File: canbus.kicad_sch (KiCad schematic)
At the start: 12 parts, among them U1 MCP2562FD, U2 MCP2518FD, Y1 40 MHz

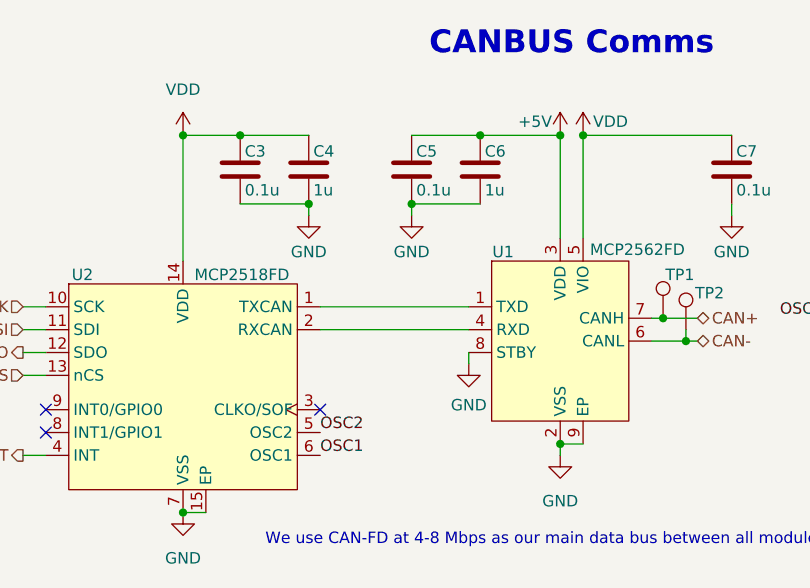
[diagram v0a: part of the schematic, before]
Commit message: Update MCP symbols to remove Exposed Pad pin.
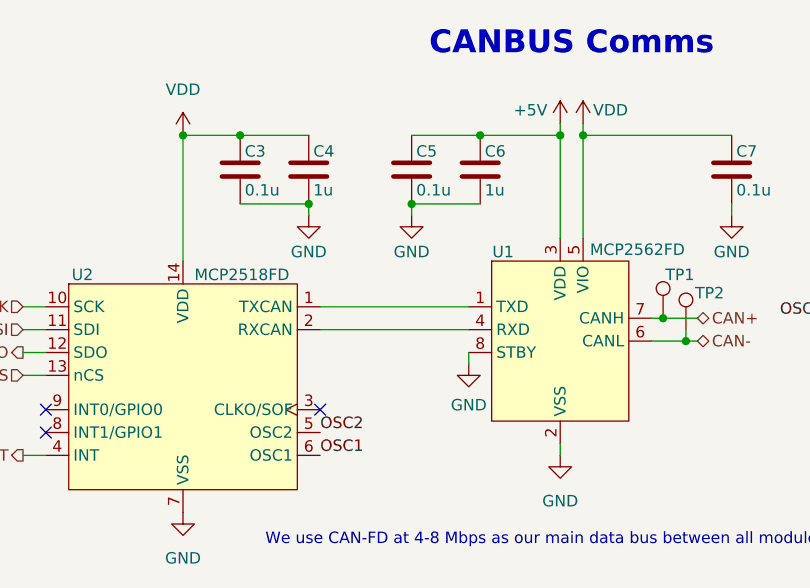
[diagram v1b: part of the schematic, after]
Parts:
- TP1, TP2: now left out of the parts list
- U1: MPN MCP2562FDT-E/SN -> MCP2562FDT-H/SN; Manufacturer Microchip Technology -> Microchip
- U2: Manufacturer Microchip Technology -> Microchip
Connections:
- net GND: no longer U1.9 (EP), U2.15 (EP)

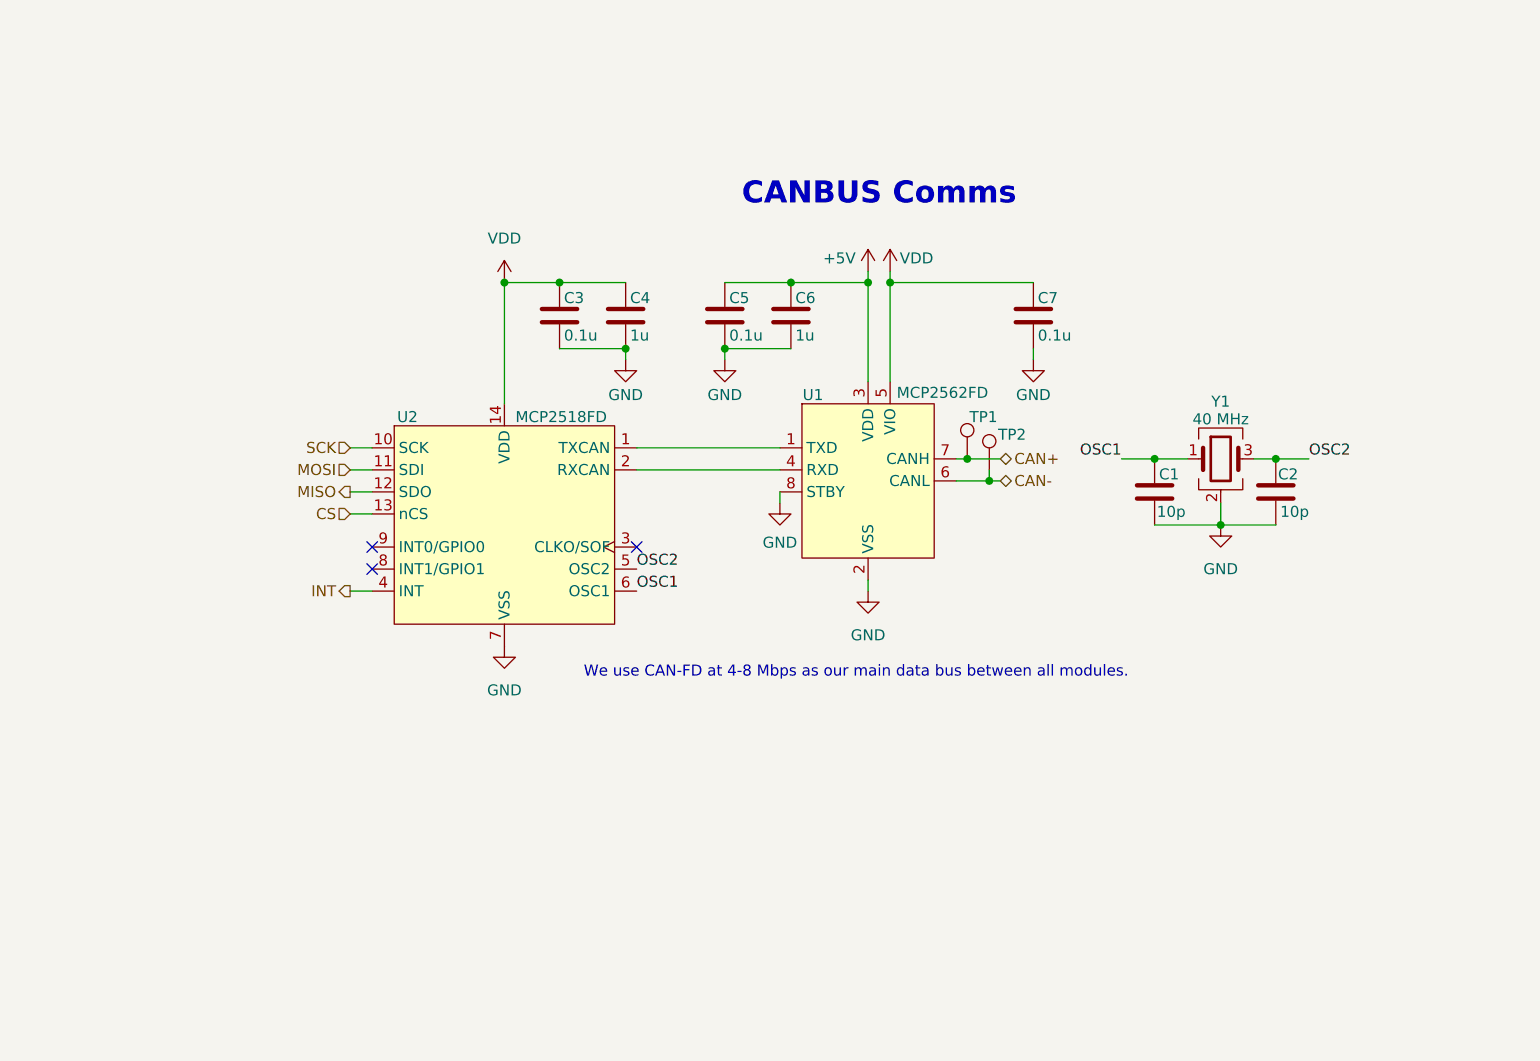
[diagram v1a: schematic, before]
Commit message: Version 3.0
This revision includes a number of changes, notably:
- larger 0805/1206 parts and reduced BOM
- SMD/TH Pads for the Pico Devboard
- Document variable Silkscreen text
- Text documentation throughout schematics
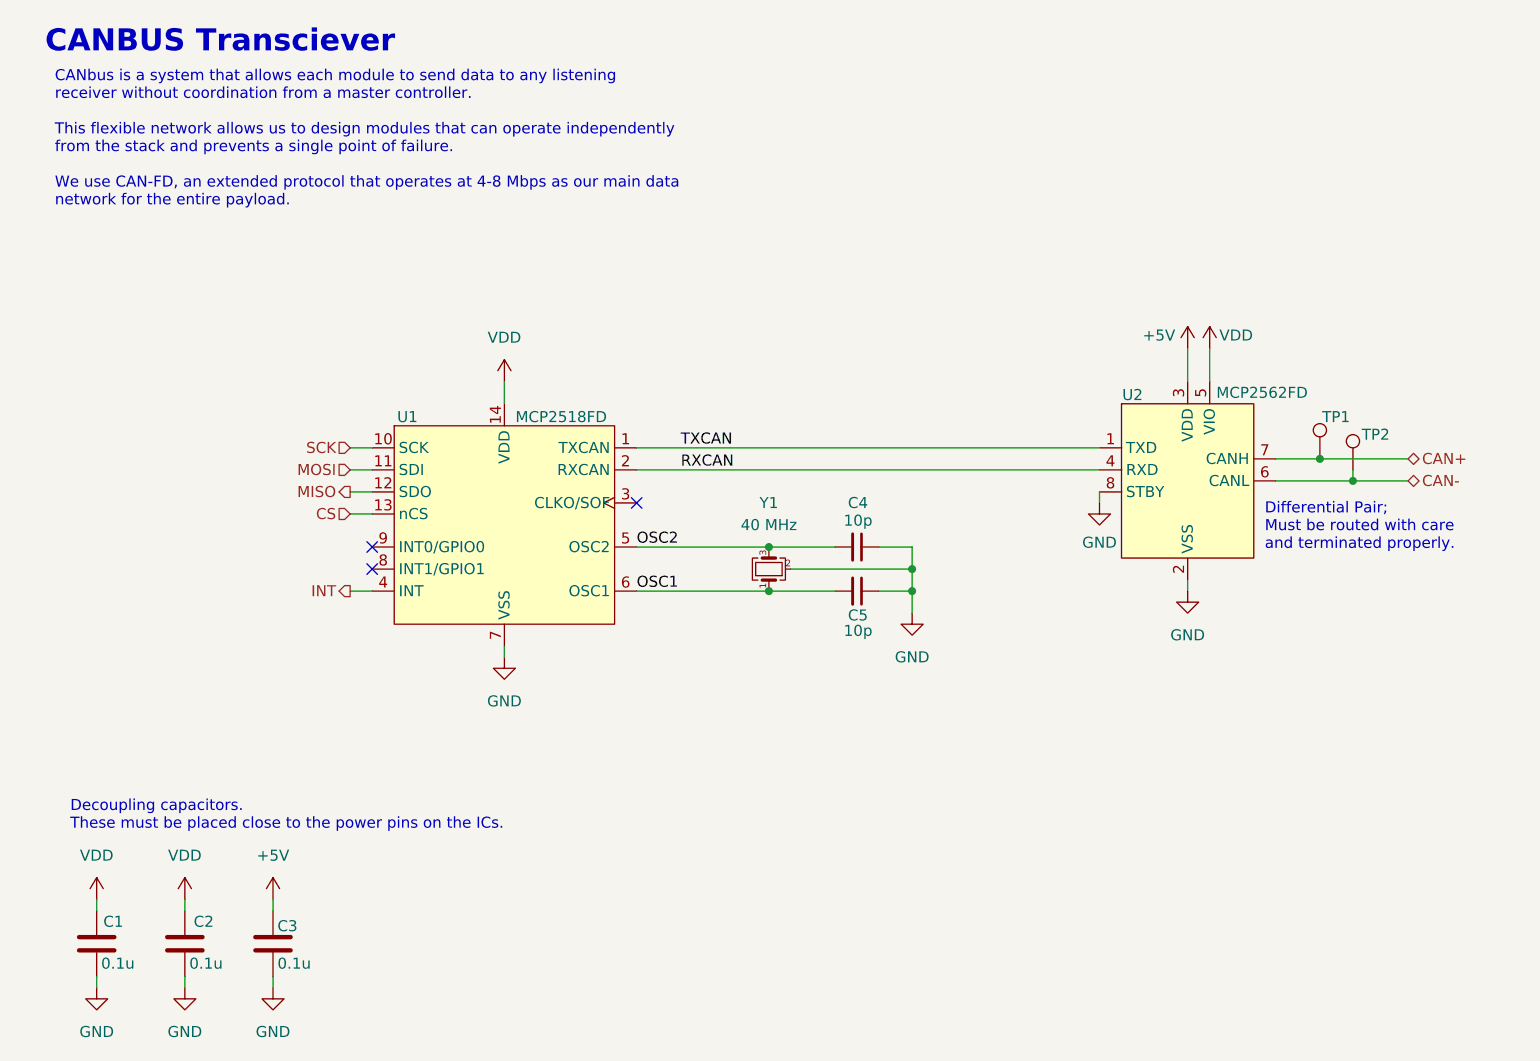
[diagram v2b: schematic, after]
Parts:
- removed C4, C6: 1u, Capacitor_SMD:C_0603_1608Metric, symbol Device:C
- removed C5, C7: 0.1u, Capacitor_SMD:C_0603_1608Metric, symbol Device:C
- added C1, C2: 0.1u, Capacitor_SMD:C_0805_2012Metric, symbol Device:C
- C3: footprint Capacitor_SMD:C_0603_1608Metric -> Capacitor_SMD:C_0805_2012Metric; Digikey 1276-CL10B104KB8NNNLCT-ND -> 1276-1003-1-ND; LCSC C913912 -> C1711; MPN CL10B104KB8NNNL -> CL21B104KBCNNNC
- C4: renamed from C2; footprint Capacitor_SMD:C_0603_1608Metric -> Capacitor_SMD:C_0805_2012Metric; symbol Device:C -> Device:C_Small; Digikey 1276-1027-1-ND -> 1276-2561-1-ND; LCSC C1634 -> C107107; MPN CL10C100JB8NNNC -> CL21C100CBANNNC
- C5: renamed from C1; footprint Capacitor_SMD:C_0603_1608Metric -> Capacitor_SMD:C_0805_2012Metric; symbol Device:C -> Device:C_Small; Digikey 1276-1027-1-ND -> 1276-2561-1-ND; LCSC C1634 -> C107107; MPN CL10C100JB8NNNC -> CL21C100CBANNNC
- Y1: symbol Device:Crystal_GND24 -> Device:Crystal_GND24_Small
- renumbered U2 to U1, U1 to U2
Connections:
- net +5V: now also C3.1
- net GND: now also C1.2, C2.2
- net VDD: now also C1.1, C2.1; no longer C3.1
- net TXCAN: now reaches U1.1 (TXCAN), U2.1 (TXD)
- net RXCAN: now reaches U1.2 (RXCAN), U2.4 (RXD)
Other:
- note added: "CANBUS Transciever"
- note added: "CANbus is a system that allows each module to send data to any listening receiver without coordination from a master controller. This flexible network allows us to design modules that can operate independently from the stack and prevents a single point of failure. We use CAN-FD, an extended protocol that operates at 4-8 Mbps as our main data network for the entire payload."
- note added: "Decoupling capacitors. These must be placed close to the power pins on the ICs."
- note added: "Differential Pair; Must be routed with care and terminated properly."
- note removed: "CANBUS Comms"
- note removed: "We use CAN-FD at 4-8 Mbps as our main data bus between all modules."
- moved on the sheet: C4, C5, TP1, TP2, U2
